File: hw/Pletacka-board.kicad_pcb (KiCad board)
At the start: 2 copper layers, 29 x 80.2 mm, 38 parts, among them J4 Conn_01x02_Female, J5 Conn_01x03_Female, SW1 SW_Push_Dual_x2, SW3 SW_Push_Dual_x2, U1 EL357N(A)(TA)-G, U2 EL357N(A)(TA)-G, U3 TPS54231D

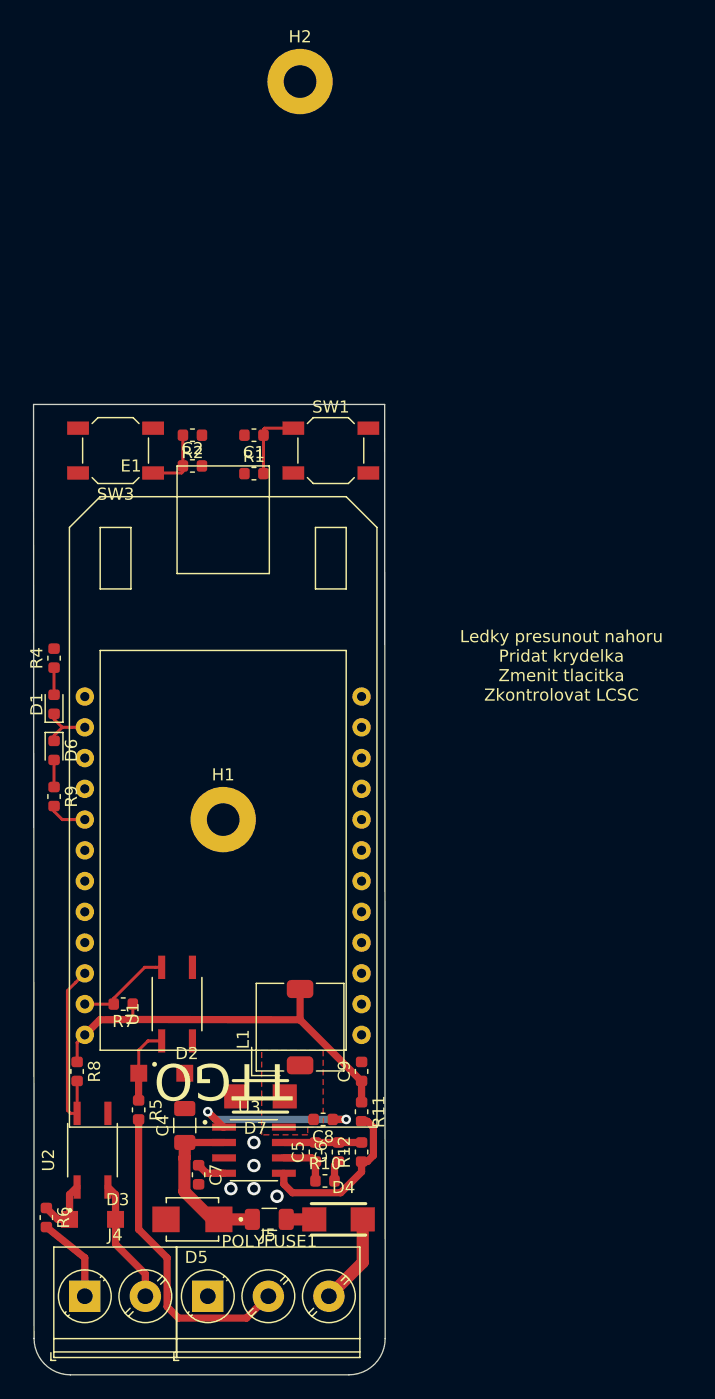
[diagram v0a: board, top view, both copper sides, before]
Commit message: Change buttons and fill ground
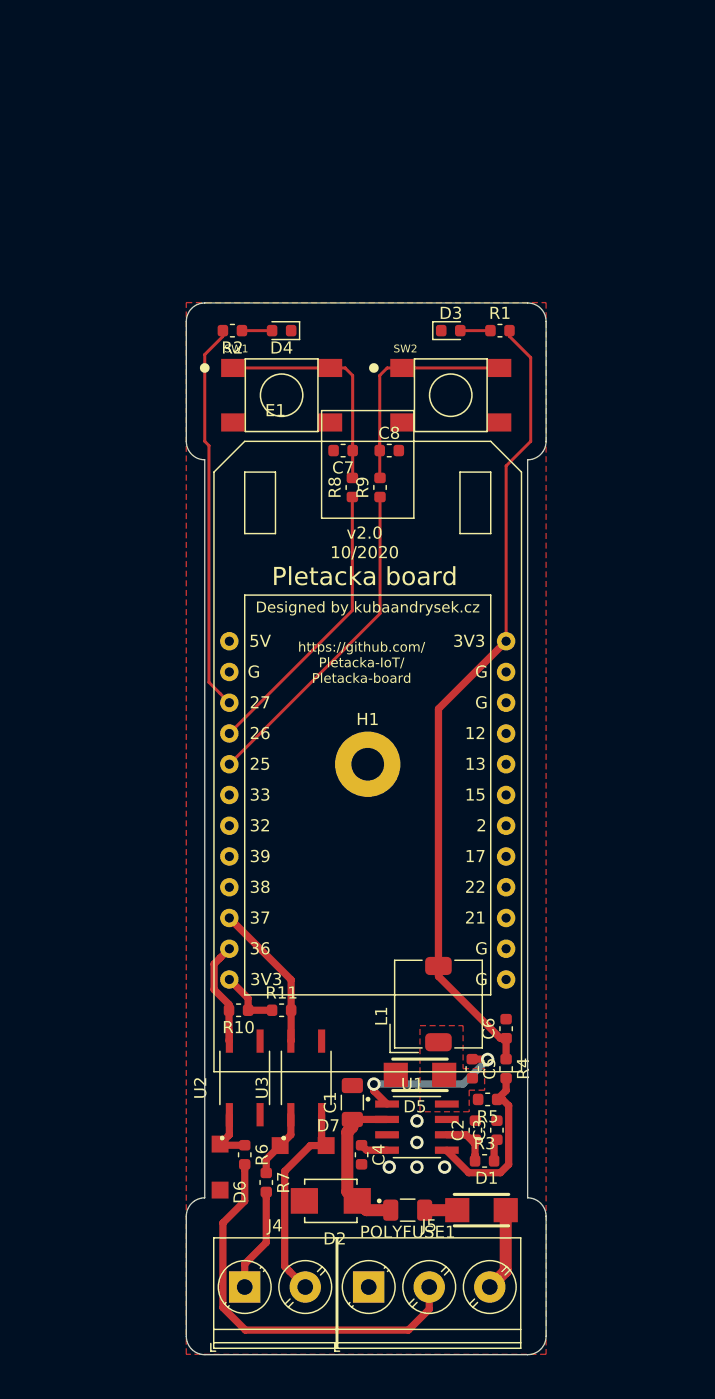
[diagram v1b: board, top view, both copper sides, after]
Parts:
- removed C9: 22u, Capacitor_SMD:C_0603_1608Metric
- removed H2: MountingHole, MountingHole:MountingHole_2.7mm_M2.5_Pad
- removed R12: R, Resistor_SMD:R_0603_1608Metric
- removed SW3: SW_Push_Dual_x2, Button_SMD:SW_SPST_SKQG_WithStem
- added C3: 22n, Capacitor_SMD:C_0603_1608Metric, F.Cu at (157.2, 129.8)
- added R3: 100-OH, Resistor_SMD:R_0603_1608Metric, F.Cu at (156.2, 132.3)
- added SW2: User_Button, Button_SMD:Button_SMD_10mm, F.Cu at (153.4, 69.1)
- C1: value 100n -> 10u/50V; footprint Capacitor_SMD:C_0603_1608Metric -> Capacitor_SMD:C_1206_3216Metric
- C2: value 100n -> 33n
- C4: value 10u/50V -> 8.2n; footprint Capacitor_SMD:C_1206_3216Metric -> Capacitor_SMD:C_0603_1608Metric
- C5: value 33n -> 100n
- C6: value 22n -> 22u
- C7: value 8.2n -> 100n
- D1: value LED -> SS34; footprint LED_SMD:LED_0603_1608Metric -> SS34:SMA
- D2: value B5819W -> 1SMB5935BT3G; footprint B5819W:B5819W_SOD-123 -> 1SMB5935BT3G:DIOM5436X247N
- D3: value B5819W -> LED; footprint B5819W:B5819W_SOD-123 -> LED_SMD:LED_0603_1608Metric
- D4: value SS34 -> LED; footprint SS34:SMA -> LED_SMD:LED_0603_1608Metric
- D5: value 1SMB5935BT3G -> SS34; footprint 1SMB5935BT3G:DIOM5436X247N -> SS34:SMA
- D6: value LED -> B5819W; footprint LED_SMD:LED_0603_1608Metric -> B5819W:B5819W_SOD-123
- D7: value SS34 -> B5819W; footprint SS34:SMA -> B5819W:B5819W_SOD-123
- J4: value Conn_01x02_Female -> STOP_INPUT
- J5: value Conn_01x03_Female -> POWER_&_FINN_INPUT
- R10: value 100-OH -> 10k
- R11: value R -> 10k
- R4: value 2k2 -> 4k7
- R5: value 20k -> 15k
- R7: value 10k -> 20k
- R8: value 10k -> 2k2
- SW1: value SW_Push_Dual_x2 -> Reset_Button; footprint Button_SMD:SW_SPST_SKQG_WithStem -> Button_SMD:Button_SMD_10mm
- U1: value EL357N(A)(TA)-G -> TPS54231D; footprint EL357N_A__TA_-G:SOP254P700X200-4N -> TPS54231D:SOIC127P599X175-8N
- U3: value TPS54231D -> EL357N(A)(TA)-G; footprint TPS54231D:SOIC127P599X175-8N -> EL357N_A__TA_-G:SOP254P700X200-4N
- moved D3 79.1 mm to (153.4, 63.8)
- moved D4 73.6 mm to (139.4, 63.8), turned to 180 degrees
- moved C7 61.0 mm to (144.5, 73.7), turned to 180 degrees
- moved C2 59.6 mm to (155.4, 129.8), turned to 90 degrees
- moved C1 55.7 mm to (145.3, 127.5), turned to 90 degrees
- moved C8 55.5 mm to (148.3, 73.7), turned to 0 degrees
- moved D1 54.7 mm to (156.0, 136.4), turned to 0 degrees
- moved R8 53.3 mm to (145.3, 76.7), turned to 90 degrees
- moved R4 50.4 mm to (158.0, 124.7), turned to 270 degrees
- moved R9 37.1 mm to (147.6, 76.7), turned to 90 degrees
- moved D6 37.0 mm to (134.4, 132.8)
- moved R5 28.8 mm to (156.5, 127.3), turned to 180 degrees
- moved R1 23.5 mm to (157.5, 63.8)
- moved D5 22.3 mm to (150.9, 125.2)
- moved U1 22.3 mm to (150.6, 129.5), turned to 0 degrees
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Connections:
- C4 pad 1: +24V -> Net-(C4-Pad1)
- C5 pad 2: GND -> Net-(C5-Pad2)
- C6 pad 1: Net-(C6-Pad1) -> +3V3
- C8 pad 2: Net-(C8-Pad2) -> GND
- D2 pad C: Net-(D2-PadC) -> Net-(C1-Pad1)
- D5 pad C: +24V -> Net-(C5-Pad2)
- D7 pad A: GND -> OPTO_STOP_IN_MINUS
- D7 pad C: Net-(C8-Pad2) -> Net-(D7-PadC)
- E1 pad 13: BTN_RESET -> Net-(E1-Pad13)
- E1 pad 21: BTN_1 -> Net-(E1-Pad21)
- E1 pad 25: LED_SEND -> BTN_USER
- E1 pad 26: Net-(E1-Pad26) -> BTN_RESET
- E1 pad 27: Net-(E1-Pad27) -> LED_USER
- L1 pad 1: Net-(C8-Pad2) -> Net-(C5-Pad2)
- POLYFUSE1 pad 1: Net-(D4-PadC) -> Net-(D1-PadC)
- POLYFUSE1 pad 2: +24V -> Net-(C1-Pad1)
- R1 pad 1: BTN_RESET -> Net-(D3-Pad2)
- R1 pad 2: Net-(C1-Pad1) -> +3V3
- R10 pad 1: Net-(C5-Pad1) -> +3V3
- R10 pad 2: Net-(C6-Pad1) -> OPTO_FINSIHED
- R11 pad 2: Net-(R11-Pad2) -> OPTO_STOP
- R2 pad 1: BTN_1 -> Net-(D4-Pad2)
- R2 pad 2: Net-(C2-Pad1) -> LED_USER
- R4 pad 1: Net-(D1-Pad2) -> +3V3
- R4 pad 2: +3V3 -> Net-(R4-Pad2)
- R5 pad 1: Net-(D2-PadC) -> Net-(R4-Pad2)
- R5 pad 2: OPTO_FINISHED_IN_PLUS -> GND
- R6 pad 1: Net-(D3-PadC) -> Net-(D6-PadC)
- R6 pad 2: OPTO_STOP_IN_PLUS -> OPTO_FINISHED_IN_PLUS
- R7 pad 1: +3V3 -> Net-(D7-PadC)
- R7 pad 2: OPTO_FINSIHED -> OPTO_STOP_IN_PLUS
- R8 pad 1: +3V3 -> BTN_RESET
- R8 pad 2: OPTO_STOP -> Net-(C7-Pad1)
- R9 pad 1: Net-(D6-Pad2) -> BTN_USER
- R9 pad 2: LED_SEND -> Net-(C8-Pad1)
- SW1 pad 1: Net-(C1-Pad1) -> Net-(C7-Pad1)
- U1 pad 1: Net-(D2-PadC) -> Net-(C5-Pad1)
- U1 pad 2: GND -> Net-(C1-Pad1)
- U1 pad 3: GND -> Net-(U1-Pad3)
- U1 pad 4: OPTO_FINSIHED -> Net-(C4-Pad1)
- U2 pad 1: Net-(D3-PadC) -> Net-(D6-PadC)
- U2 pad 2: OPTO_STOP_IN_MINUS -> GND
- U2 pad 4: OPTO_STOP -> OPTO_FINSIHED
- U3 pad 1: Net-(C8-Pad1) -> Net-(D7-PadC)
- U3 pad 2: +24V -> OPTO_STOP_IN_MINUS
- U3 pad 3: Net-(U3-Pad3) -> GND
- U3 pad 4: Net-(C7-Pad1) -> OPTO_STOP
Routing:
- net +3V3: track 33.6 -> 71.8 mm
- net LED_USER: track 0.00 -> 32.2 mm
- net BTN_USER: track 0.00 -> 27.2 mm
- net BTN_RESET: track 0.00 -> 23.7 mm
- net Net-(C7-Pad1): track 2.38 -> 18.6 mm
- net Net-(R4-Pad2): track 0.00 -> 14.3 mm
- net +24V: track 13.9 -> 0.00 mm
- net Net-(R11-Pad2): track 13.9 -> 0.00 mm
- net GND: track 11.1 -> 0.00 mm
- net Net-(C5-Pad1): track 4.34 -> 13.6 mm, vias 0 -> 2
- net OPTO_FINISHED_IN_PLUS: track 25.9 -> 32.9 mm
- net OPTO_STOP_IN_MINUS: track 10.3 -> 17.3 mm
- net Net-(C1-Pad1): track 6.16 -> 13.0 mm
- net Net-(D2-PadC): track 6.36 -> 0.00 mm
- net Net-(D7-PadC): track 0.00 -> 5.65 mm
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- added copper zone on F.Cu, net GND
- added copper zone on F.Cu, net Net-(C5-Pad2)
- removed copper zone on F.Cu, net Net-(C8-Pad2)
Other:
- board size 29 x 80.2 mm -> 29.7 x 86.9 mm
- board text added: "Designed by kubaandrysek.cz"
- board text added: "Pletacka board"
- board text added: "https://github.com/ Pletacka-IoT/ Pletacka-board"
- board text added: "v2.0 10/2020"
- board text removed: "Ledky presunout nahoru Pridat krydelka Zmenit tlacitka Zkontrolovat LCSC"
